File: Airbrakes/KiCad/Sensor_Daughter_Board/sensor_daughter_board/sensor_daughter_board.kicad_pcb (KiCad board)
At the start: 2 copper layers, 28 x 12 mm, 11 parts, among them U1 BMI088, U2 BMP581, U3 BMM350

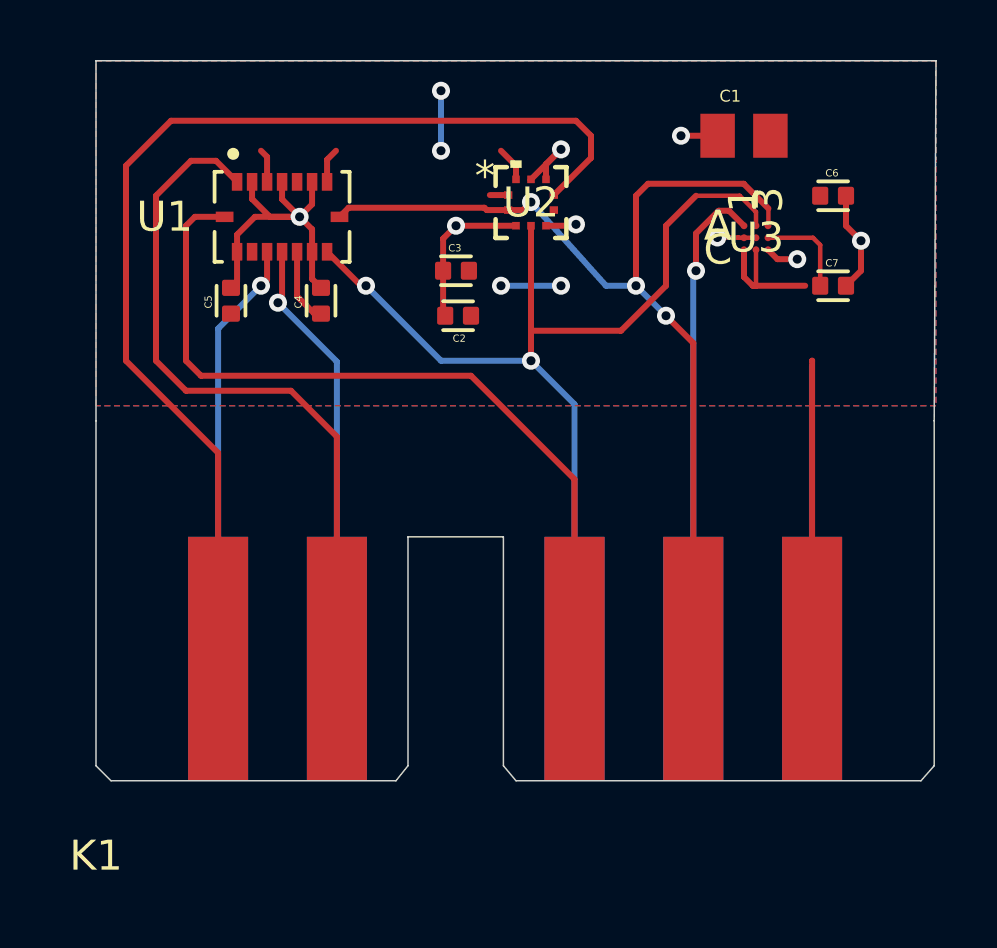
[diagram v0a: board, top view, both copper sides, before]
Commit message: Reroute/tweak few traces + DRC solder mask modification
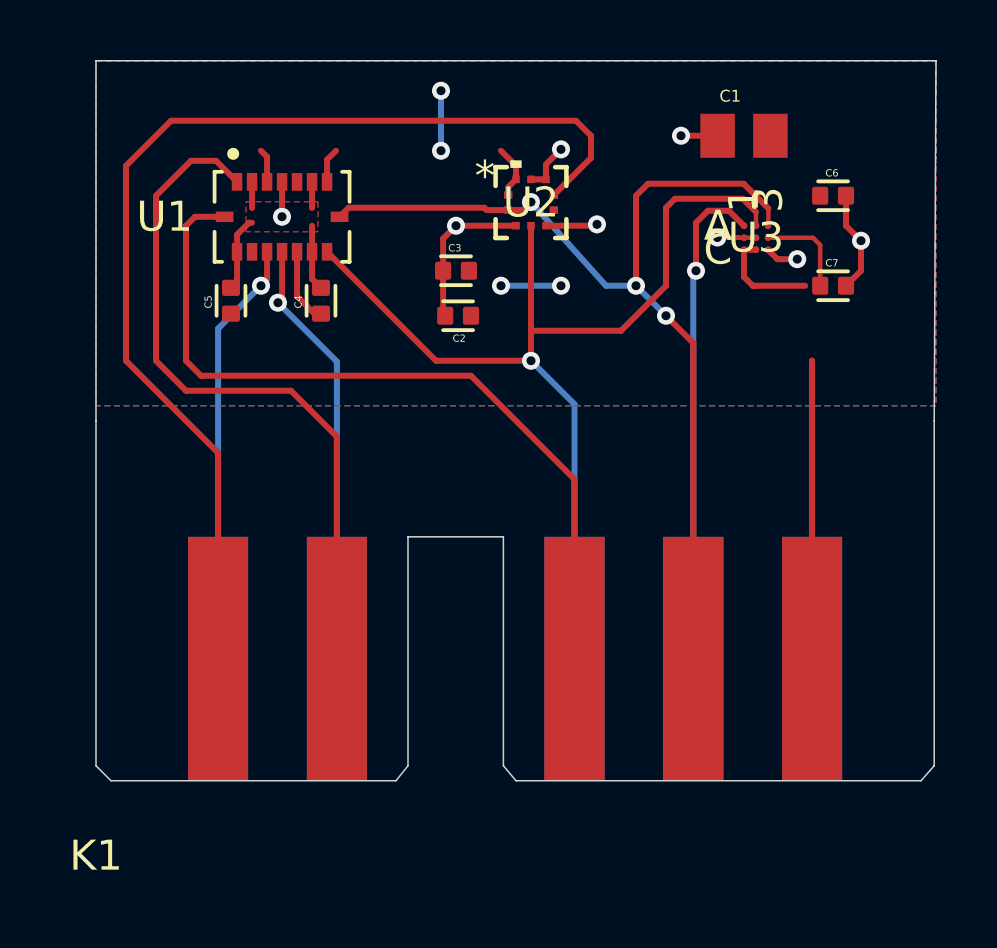
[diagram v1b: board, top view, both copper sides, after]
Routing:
- net GND: track 37.2 -> 32.9 mm
- net +3V3: track 27.5 -> 26.7 mm
- net SDA: track 34.6 -> 34.8 mm, vias 2 -> 1
- added copper zone on F.Cu, net GND

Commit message: Fix DRC unconnections
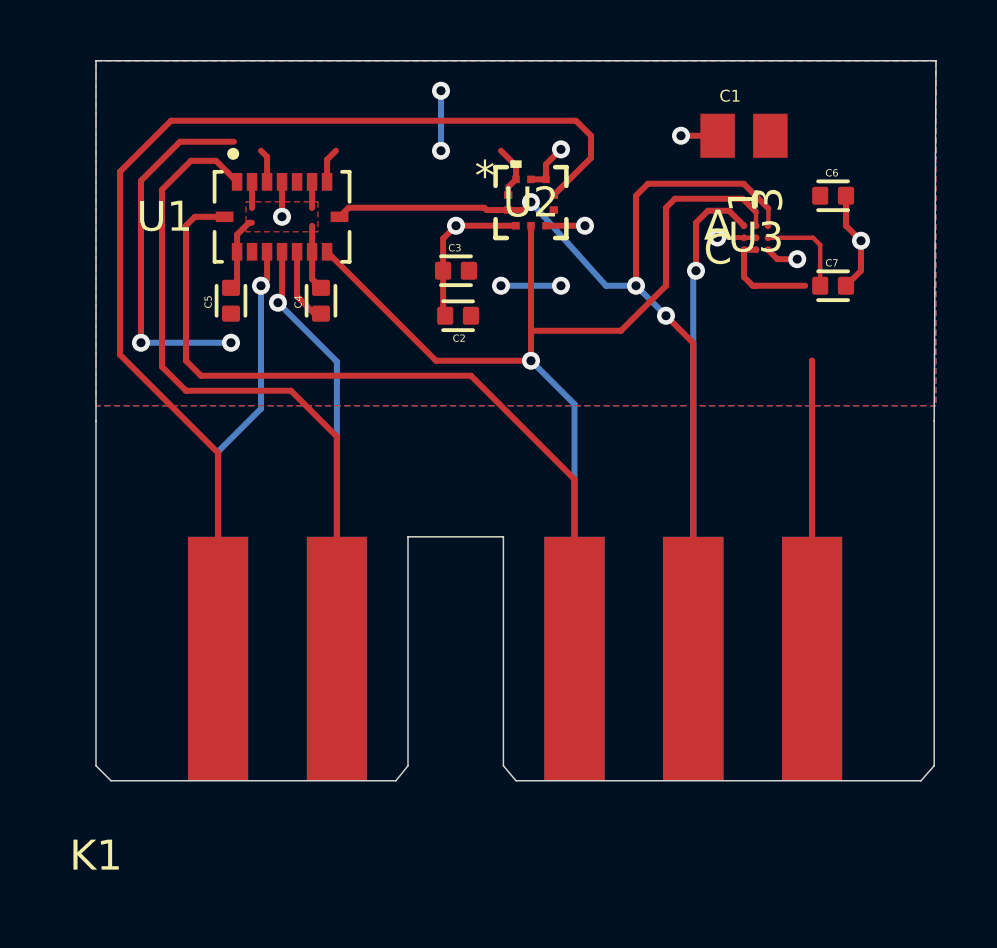
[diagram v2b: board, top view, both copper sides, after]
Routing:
- net +3V3: track 26.7 -> 38.7 mm, vias 4 -> 6
- net GYRO_INT_2: track 13.7 -> 14.2 mm
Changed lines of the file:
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@@
-	)
-	(segment
-		(start 111.7 42.453998)
-		(end 111.653998 42.5)
-		(width 0.2)
-		(layer "F.Cu")
-		(net 3)
 	)
 	(segment
@@
 	)
 	(segment
+		(start 111.3 42.5)
+		(end 109.999999 42.5)
+		(width 0.2)
+		(layer "F.Cu")
+		(net 3)
+	)
+	(segment
 		(start 101.2025 41.5975)
 		(end 101.2 41.6)
@@
 	)
 	(segment
-		(start 111.653998 42.5)
-		(end 109.999999 42.5)
-		(width 0.2)
-		(layer "F.Cu")
-		(net 3)
-	)
-	(segment
 		(start 100.2025 41.0375)
 		(end 100.2025 41.8975)
@@
 	)
 	(via
-		(at 111.7 42.453998)
+		(at 111.3 42.5)
 		(size 0.6)
 		(drill 0.3)
@@
 	)
 	(segment
+		(start 99.6 39.7)
+		(end 97.8 39.7)
+		(width 0.2)
+		(layer "F.Cu")
+		(net 5)
+	)
+	(segment
 		(start 116.59995 44.20715)
 		(end 116.59995 43.31435)
@@
 		(start 101.7025 44.853971)
 		(end 101.7025 43.3675)
+		(width 0.2)
+		(layer "F.Cu")
+		(net 5)
+	)
+	(segment
+		(start 96.5 41)
+		(end 96.5 41.2)
+		(width 0.2)
+		(layer "F.Cu")
+		(net 5)
+	)
+	(segment
+		(start 96.5 43.5)
+		(end 96.5 46.4)
 		(width 0.2)
 		(layer "F.Cu")
@@
 	)
 	(segment
+		(start 97.8 39.7)
+		(end 96.5 41)
+		(width 0.2)
+		(layer "F.Cu")
+		(net 5)
+	)
+	(segment
 		(start 117.40005 42.90005)
 		(end 118.90005 42.90005)
@@
 	)
 	(segment
+		(start 96.5 41.2)
+		(end 96.5 43.5)
+		(width 0.2)
+		(layer "F.Cu")
+		(net 5)
+	)
+	(segment
 		(start 118.87 56.435)
 		(end 118.87 46.999125)
@@
 		(net 5)
 	)
+	(via
+		(at 99.5 46.4)
+		(size 0.6)
+		(drill 0.3)
+		(layers "F.Cu" "B.Cu")
+		(net 5)
+	)
+	(via
+		(at 96.5 46.4)
+		(size 0.6)
+		(drill 0.3)
+		(layers "F.Cu" "B.Cu")
+		(net 5)
+	)
+	(segment
+		(start 96.5 46.4)
+		(end 99.5 46.4)
+		(width 0.2)
+		(layer "B.Cu")
+		(net 5)
+	)
 	(segment
 		(start 106.5 38)
@@
 	)
 	(segment
-		(start 99.07 45.93)
+		(start 99.07 56.935)
+		(end 99.07 50.03)
+		(width 0.2)
+		(layer "B.Cu")
+		(net 8)
+	)
+	(segment
+		(start 100.5 48.6)
 		(end 100.5 44.5)
 		(width 0.2)
@@
 	)
 	(segment
-		(start 99.07 56.435)
-		(end 99.07 45.93)
+		(start 99.07 50.03)
+		(end 100.5 48.6)
 		(width 0.2)
 		(layer "B.Cu")
 		(net 8)
+	)
+	(segment
+		(start 98.165 40.335)
+		(end 99 40.335)
+		(width 0.2)
+		(layer "F.Cu")
+		(net 9)
+	)
+	(segment
+		(start 103.03 49.53)
+		(end 101.5 48)
+		(width 0.2)
+		(layer "F.Cu")
+		(net 9)
+	)
+	(segment
+		(start 101.5 48)
+		(end 98 48)
+		(width 0.2)
+		(layer "F.Cu")
+		(net 9)
+	)
+	(segment
+		(start 97.2 47.2)
+		(end 97.2 41.3)
+		(width 0.2)
+		(layer "F.Cu")
+		(net 9)
+	)
+	(segment
+		(start 103.03 56.435)
+		(end 103.03 49.53)
+		(width 0.2)
+		(layer "F.Cu")
+		(net 9)
+	)
+	(segment
+		(start 98 48)
+		(end 97.2 47.2)
+		(width 0.2)
+		(layer "F.Cu")
+		(net 9)
 	)
 	(segment
@@
 	)
 	(segment
-		(start 103.03 50.03)
-		(end 103.03 49.53)
+		(start 97.2 41.3)
+		(end 98.165 40.335)
 		(width 0.2)
 		(layer "F.Cu")
@@
 	)
 	(segment
-		(start 97 41.5)
-		(end 98.165 40.335)
-		(width 0.2)
-		(layer "F.Cu")
-		(net 9)
-	)
-	(segment
-		(start 98 48)
-		(end 97 47)
-		(width 0.2)
-		(layer "F.Cu")
-		(net 9)
-	)
-	(segment
-		(start 103.03 51.03)
-		(end 103.03 50.03)
-		(width 0.2)
-		(layer "F.Cu")
-		(net 9)
-	)
-	(segment
-		(start 97 47)
-		(end 97 41.5)
-		(width 0.2)
-		(layer "F.Cu")
-		(net 9)
-	)
-	(segment
-		(start 98.165 40.335)
-		(end 99 40.335)
-		(width 0.2)
-		(layer "F.Cu")
-		(net 9)
-	)
-	(segment
-		(start 101.5 48)
-		(end 98 48)
-		(width 0.2)
-		(layer "F.Cu")
-		(net 9)
-	)
-	(segment
-		(start 103.03 49.53)
-		(end 101.5 48)
-		(width 0.2)
-		(layer "F.Cu")
-		(net 9)
-	)
-	(segment
-		(start 103.03 56.435)
-		(end 103.03 51.03)
-		(width 0.2)
-		(layer "F.Cu")
-		(net 9)
+		(start 95.8 40.7)
+		(end 97.5 39)
+		(width 0.2)
+		(layer "F.Cu")
+		(net 13)
 	)
 	(segment
@@
 	)
 	(segment
+		(start 99.07 50.07)
+		(end 95.8 46.8)
+		(width 0.2)
+		(layer "F.Cu")
+		(net 13)
+	)
+	(segment
+		(start 111 39)
+		(end 111.5 39.5)
+		(width 0.2)
+		(layer "F.Cu")
+		(net 13)
+	)
+	(segment
+		(start 111.5 39.5)
+		(end 111.5 40.2373)
+		(width 0.2)
+		(layer "F.Cu")
+		(net 13)
+	)
+	(segment
+		(start 95.8 46.8)
+		(end 95.8 40.7)
+		(width 0.2)
+		(layer "F.Cu")
+		(net 13)
+	)
+	(segment
 		(start 97.5 39)
 		(end 111 39)
@@
 	)
 	(segment
-		(start 96 47)
-		(end 96 40.5)
-		(width 0.2)
-		(layer "F.Cu")
-		(net 13)
-	)
-	(segment
 		(start 111.5 40.2373)
 		(end 110.260301 41.476999)
 		(width 0.2)
 		(layer "F.Cu")
-		(net 13)
-	)
-	(segment
-		(start 111 39)
-		(end 111.5 39.5)
-		(width 0.2)
-		(layer "F.Cu")
-		(net 13)
-	)
-	(segment
-		(start 99.07 50.07)
-		(end 96 47)
-		(width 0.2)
-		(layer "F.Cu")
-		(net 13)
-	)
-	(segment
-		(start 96 40.5)
-		(end 97.5 39)
-		(width 0.2)
-		(layer "F.Cu")
-		(net 13)
-	)
-	(segment
-		(start 111.5 39.5)
-		(end 111.5 40.2373)
-		(width 0.2)
-		(layer "F.Cu")
